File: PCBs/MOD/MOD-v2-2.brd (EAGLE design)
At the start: 138.8 x 49.3 mm, 32 parts, among them J1 SERVO1, J10 JOY1, J11 JOY2, J2 SERVO2, J4 ACTUATORS, J5 POWER-5V, J6 AN5, J7 AN6, J8 AN7, J9 AN8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

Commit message: added RPi power control circuitry
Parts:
- removed SW1: 500SSP1S2M2QEA, CMU-ArtFab:SWITCH_SPDT_500SSP1S2M2QEA
- added J12: RPi-Reset, SparkFun-Connectors:1X02_LOCK
- added J3: RPi, adafruit:DCJACK_2MM_PTH
- added R2: 2.2k, resistor:0204/7
- added R3: 3.3k, resistor:0204/7
- added RELAY1: RELAY-OMRON-G6DN, CMU-ArtFab:G6DN-1A
- added SW2: 500SSP1S2M2QEA, CMU-ArtFab:SWITCH_SPDT_500SSP1S2M2QEA
- added U1: ATTINY85SU, attiny85:ATTINY85
- J5: value POWER-5V -> Battery
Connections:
- removed net N$1: J5.PWR, SW1.2
- new net +5V-BATTERY: J5.PWR, RELAY1.5, SW2.1, U1.8
- new net +5V-PI: J3.PWR, RELAY1.8
- new net N$3: SW2.2, U1.5
- new net N$4: RELAY1.1, U1.7
- new net N$5: J12.1, R2.1, R3.2
- new net PI-REST: R2.2, U1.6
- net +5V: now also U1.3; no longer SW1.1
- net GND: now also J12.2, J3.GND, R3.1, RELAY1.2, SW2.3, U1.4
- net GNDBREAK: now also J3.GNDBREAK
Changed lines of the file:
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@@
 <?xml version="1.0" encoding="utf-8"?>
 <!DOCTYPE eagle SYSTEM "eagle.dtd">
-<eagle version="8.2.2">
+<eagle version="8.3.1">
 <drawing>
 <settings>
 <setting alwaysvectorfont="no"/>
+<setting keepoldvectorfont="yes"/>
 <setting verticaltext="up"/>
 </settings>
@@
 <attribute name="VALUE" x="139.381" y="30.868" size="1.016" layer="28" font="vector" ratio="20" rot="MR270"/>
 </element>
-<element name="J5" library="adafruit" package="DCJACK_2MM_PTH" value="POWER-5V" x="139.612" y="41.774" smashed="yes" rot="MR270">
+<element name="J5" library="adafruit" package="DCJACK_2MM_PTH" value="Battery" x="139.612" y="41.774" smashed="yes" rot="MR270">
 <attribute name="NAME" x="126.912" y="46.727" size="1.016" layer="26" font="vector" ratio="15" rot="MR0"/>
 <attribute name="VALUE" x="135.294" y="46.727" size="1.016" layer="28" font="vector" ratio="15" rot="MR0"/>
@@
 <attribute name="NAME" x="73.57799375" y="4.424896875" size="0.9906" layer="26" ratio="10" rot="MR270"/>
 <attribute name="VALUE" x="75.5356" y="7.102603125" size="0.9906" layer="28" ratio="10" rot="MR270"/>
-</element>
-<element name="SW1" library="CMU-ArtFab" package="SWITCH_SPDT_500SSP1S2M2QEA" value="500SSP1S2M2QEA" x="68.804" y="6.477" rot="R270">
-<attribute name="DIGIKEY" value="EG5137-ND" x="68.804" y="6.477" size="1.016" layer="27" font="vector" ratio="15" rot="R270" display="off"/>
 </element>
 <element name="TEENSY" library="CMU-ArtFab" package="TEENSY3-6_NO-USB-HOST" value="TEENSY3_6-ALI_NO-USB-HOST" x="99.904" y="18.34" rot="MR0"/>
@@
 <element name="S3" library="CMU-ArtFab" package="SWITCH_TR2-MOMENTARY-LED" value="SW-LEDPTH" x="108" y="4"/>
 <element name="S4" library="CMU-ArtFab" package="SWITCH_TR2-MOMENTARY-LED" value="SW-LEDPTH" x="128" y="4"/>
+<element name="U1" library="attiny85" package="ATTINY85" value="ATTINY85SU" x="-21" y="-4"/>
+<element name="RELAY1" library="CMU-ArtFab" package="G6DN-1A" value="RELAY-OMRON-G6DN" x="-21" y="-18"/>
+<element name="J3" library="adafruit" package="DCJACK_2MM_PTH" value="RPi" x="-50" y="-13"/>
+<element name="SW2" library="CMU-ArtFab" package="SWITCH_SPDT_500SSP1S2M2QEA" value="500SSP1S2M2QEA" x="-54" y="-38">
+<attribute name="DIGIKEY" value="EG5137-ND" x="-54" y="-38" size="1.778" layer="27" display="off"/>
+</element>
+<element name="R2" library="resistor" library_urn="urn:adsk.eagle:library:348" package="0204/7" value="2.2k" x="-60" y="-57"/>
+<element name="R3" library="resistor" library_urn="urn:adsk.eagle:library:348" package="0204/7" value="3.3k" x="-60" y="-71"/>
+<element name="J12" library="SparkFun-Connectors" library_urn="urn:adsk.eagle:library:513" package="1X02_LOCK" package3d_urn="urn:adsk.eagle:package:38045/1" value="RPi-Reset" x="-61" y="-88"/>
 </elements>
 <signals>
@@
 <contactref element="J2" pad="1"/>
 <contactref element="J4" pad="10"/>
-<contactref element="J5" pad="GND"/>
-<contactref element="LED1" pad="K"/>
 <contactref element="TEENSY" pad="G2"/>
 <contactref element="TEENSY" pad="G3"/>
@@
 <contactref element="S4" pad="C"/>
 <contactref element="S4" pad="1"/>
+<contactref element="U1" pad="4"/>
+<contactref element="RELAY1" pad="2"/>
+<contactref element="J5" pad="GND"/>
+<contactref element="SW2" pad="3"/>
+<contactref element="LED1" pad="K"/>
+<contactref element="J3" pad="GND"/>
+<contactref element="R3" pad="1"/>
+<contactref element="J12" pad="2"/>
+<wire x1="128.119" y1="32.99" x2="132.262" y2="41.774" width="0" layer="19" extent="1-1"/>
+<wire x1="125.539" y1="32.94" x2="128.119" y2="32.99" width="0" layer="19" extent="1-1"/>
+<wire x1="116.447" y1="32.377" x2="125.539" y2="32.94" width="0" layer="19" extent="1-1"/>
+<wire x1="118.65" y1="43.187" x2="116.447" y2="32.377" width="0" layer="19" extent="1-1"/>
+<wire x1="98.18" y1="43.187" x2="118.65" y2="43.187" width="0" layer="19" extent="1-1"/>
+<wire x1="77.69" y1="43.177" x2="98.18" y2="43.187" width="0" layer="19" extent="1-1"/>
+<wire x1="63.074" y1="34.85" x2="77.69" y2="43.177" width="0" layer="19" extent="1-1"/>
+<wire x1="57.22" y1="43.177" x2="63.074" y2="34.85" width="0" layer="19" extent="1-1"/>
+<wire x1="52.914" y1="27.23" x2="63.074" y2="34.85" width="0" layer="19" extent="1-1"/>
+<wire x1="40.214" y1="27.23" x2="52.914" y2="27.23" width="0" layer="19" extent="1-1"/>
+<wire x1="36.79" y1="43.157" x2="40.214" y2="27.23" width="0" layer="19" extent="1-1"/>
+<wire x1="83.394" y1="27.23" x2="77.69" y2="43.177" width="0" layer="19" extent="1-1"/>
+<wire x1="98.634" y1="19.61" x2="83.394" y2="27.23" width="0" layer="19" extent="1-1"/>
+<wire x1="89.8" y1="11.205" x2="98.634" y2="19.61" width="0" layer="19" extent="16-16"/>
+<wire x1="68.824" y1="16.619" x2="83.394" y2="27.23" width="0" layer="19" extent="1-1"/>
+<wire x1="108" y1="1.46" x2="98.634" y2="19.61" width="0" layer="19" extent="1-1"/>
+<wire x1="110.54" y1="1.46" x2="108" y2="1.46" width="0" layer="19" extent="1-1"/>
+<wire x1="128" y1="1.46" x2="110.54" y2="1.46" width="0" layer="19" extent="1-1"/>
+<wire x1="130.54" y1="1.46" x2="128" y2="1.46" width="0" layer="19" extent="1-1"/>
+<wire x1="16.36" y1="43.157" x2="36.79" y2="43.157" width="0" layer="19" extent="1-1"/>
+<wire x1="49.14" y1="2.255" x2="68.824" y2="16.619" width="0" layer="19" extent="16-16"/>
+<wire x1="32.54" y1="2.46" x2="49.14" y2="2.255" width="0" layer="19" extent="16-16"/>
+<wire x1="30" y1="2.46" x2="32.54" y2="2.46" width="0" layer="19" extent="1-1"/>
+<wire x1="12.54" y1="2.46" x2="30" y2="2.46" width="0" layer="19" extent="1-1"/>
+<wire x1="10" y1="2.46" x2="12.54" y2="2.46" width="0" layer="19" extent="1-1"/>
+<wire x1="-19.095" y1="-7.33" x2="10" y2="2.46" width="0" layer="19" extent="1-1"/>
+<wire x1="-18.46" y1="-18" x2="-19.095" y2="-7.33" width="0" layer="19" extent="1-1"/>
+<wire x1="-50" y1="-5.65" x2="-19.095" y2="-7.33" width="0" layer="19" extent="1-1"/>
+<wire x1="-49.3" y1="-38" x2="-50" y2="-5.65" width="0" layer="19" extent="1-1"/>
+<wire x1="-63.81" y1="-71" x2="-49.3" y2="-38" width="0" layer="19" extent="1-1"/>
+<wire x1="-58.2822" y1="-88" x2="-63.81" y2="-71" width="0" layer="19" extent="1-1"/>
 </signal>
 <signal name="B1">
@@
 <contactref element="J4" pad="7"/>
 <contactref element="J4" pad="8"/>
+<contactref element="U1" pad="3"/>
 <contactref element="R1" pad="2"/>
-<contactref element="SW1" pad="1"/>
+<wire x1="125.285" y1="30.4" x2="127.865" y2="30.45" width="0" layer="19" extent="1-1"/>
+<wire x1="113.907" y1="29.583" x2="125.285" y2="30.4" width="0" layer="19" extent="1-1"/>
+<wire x1="113.907" y1="32.377" x2="113.907" y2="29.583" width="0" layer="19" extent="1-1"/>
+<wire x1="75.053" y1="1.667" x2="113.907" y2="29.583" width="0" layer="19" extent="1-1"/>
+<wire x1="-20.365" y1="-7.33" x2="75.053" y2="1.667" width="0" layer="19" extent="1-1"/>
 </signal>
 <signal name="S1">
@@
 <signal name="GNDBREAK">
 <contactref element="J5" pad="GNDBREAK"/>
-</signal>
-<signal name="N$1">
-<contactref element="J5" pad="PWR"/>
-<contactref element="SW1" pad="2"/>
-<wire x1="68.804" y1="6.477" x2="126.012" y2="41.774" width="0" layer="19" extent="1-1"/>
+<contactref element="J3" pad="GNDBREAK"/>
+<wire x1="-45.2" y1="-2.25" x2="128.862" y2="36.974" width="0" layer="19" extent="1-1"/>
 </signal>
 <signal name="N$2">
@@
 <contactref element="U$1" pad="9"/>
 <contactref element="U$2" pad="9"/>
+<wire x1="58.74" y1="2.255" x2="80.2" y2="11.205" width="0" layer="19" extent="16-16"/>
 </signal>
 <signal name="N$11">
@@
 <contactref element="TEENSY" pad="46"/>
 <wire x1="42.754" y1="27.23" x2="108.827" y2="32.377" width="0" layer="19" extent="1-1"/>
+</signal>
+<signal name="N$3">
+<contactref element="U1" pad="5"/>
+<contactref element="SW2" pad="2"/>
+<wire x1="-19.095" y1="-0.67" x2="-54" y2="-38" width="0" layer="19" extent="1-1"/>
+</signal>
+<signal name="+5V-PI">
+<contactref element="RELAY1" pad="8"/>
+<contactref element="J3" pad="PWR"/>
+<wire x1="-3.22" y1="-18" x2="-50" y2="0.6" width="0" layer="19" extent="1-1"/>
+</signal>
+<signal name="PI-REST">
+<contactref element="U1" pad="6"/>
+<contactref element="R2" pad="2"/>
+<wire x1="-20.365" y1="-0.67" x2="-56.19" y2="-57" width="0" layer="19" extent="1-1"/>
+</signal>
+<signal name="+5V-BATTERY">
+<contactref element="U1" pad="8"/>
+<contactref element="J5" pad="PWR"/>
+<contactref element="SW2" pad="1"/>
+<contactref element="RELAY1" pad="5"/>
+<wire x1="-10.84" y1="-18" x2="126.012" y2="41.774" width="0" layer="19" extent="1-1"/>
+<wire x1="-22.905" y1="-0.67" x2="-10.84" y2="-18" width="0" layer="19" extent="1-1"/>
+<wire x1="-58.7" y1="-38" x2="-22.905" y2="-0.67" width="0" layer="19" extent="1-1"/>
+</signal>
+<signal name="N$4">
+<contactref element="U1" pad="7"/>
+<contactref element="RELAY1" pad="1"/>
+<wire x1="-21.635" y1="-0.67" x2="-21" y2="-18" width="0" layer="19" extent="1-1"/>
+</signal>
+<signal name="N$5">
+<contactref element="R2" pad="1"/>
+<contactref element="R3" pad="2"/>
+<contactref element="J12" pad="1"/>
+<wire x1="-56.19" y1="-71" x2="-61.1778" y2="-88" width="0" layer="19" extent="1-1"/>
+<wire x1="-63.81" y1="-57" x2="-56.19" y2="-71" width="0" layer="19" extent="1-1"/>
 </signal>
 </signals>
@@
 </note>
 <note version="8.2" severity="warning">
-Since Version 8.2, Eagle supports online libraries. The ids
+Since Version 8.2, EAGLE supports online libraries. The ids
 of those online libraries will not be understood (or retained)
 with this version.
 </note>
+<note version="8.3" severity="warning">
+Since Version 8.3, EAGLE supports URNs for individual library
+assets (packages, symbols, and devices). The URNs of those assets
+will not be understood (or retained) with this version.
+</note>
+<note version="8.3" severity="warning">
+Since Version 8.3, EAGLE supports the association of 3D packages
+with devices in libraries, schematics, and board files. Those 3D
+packages will not be understood (or retained) with this version.
+</note>
 </compatibility>

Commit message: added RPi power control circuitry
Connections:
- removed net +5V-PI: J3.PWR, RELAY1.8
- net +5V: now also J3.PWR, RELAY1.8
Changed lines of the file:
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@@
 <contactref element="U1" pad="3"/>
 <contactref element="R1" pad="2"/>
+<contactref element="RELAY1" pad="8"/>
+<contactref element="J3" pad="PWR"/>
 <wire x1="125.285" y1="30.4" x2="127.865" y2="30.45" width="0" layer="19" extent="1-1"/>
 <wire x1="113.907" y1="29.583" x2="125.285" y2="30.4" width="0" layer="19" extent="1-1"/>
 <wire x1="113.907" y1="32.377" x2="113.907" y2="29.583" width="0" layer="19" extent="1-1"/>
 <wire x1="75.053" y1="1.667" x2="113.907" y2="29.583" width="0" layer="19" extent="1-1"/>
-<wire x1="-20.365" y1="-7.33" x2="75.053" y2="1.667" width="0" layer="19" extent="1-1"/>
+<wire x1="-3.22" y1="-18" x2="75.053" y2="1.667" width="0" layer="19" extent="1-1"/>
+<wire x1="-20.365" y1="-7.33" x2="-3.22" y2="-18" width="0" layer="19" extent="1-1"/>
+<wire x1="-50" y1="0.6" x2="-20.365" y2="-7.33" width="0" layer="19" extent="1-1"/>
 </signal>
 <signal name="S1">
@@
 <wire x1="-19.095" y1="-0.67" x2="-54" y2="-38" width="0" layer="19" extent="1-1"/>
 </signal>
-<signal name="+5V-PI">
-<contactref element="RELAY1" pad="8"/>
-<contactref element="J3" pad="PWR"/>
-<wire x1="-3.22" y1="-18" x2="-50" y2="0.6" width="0" layer="19" extent="1-1"/>
-</signal>
 <signal name="PI-REST">

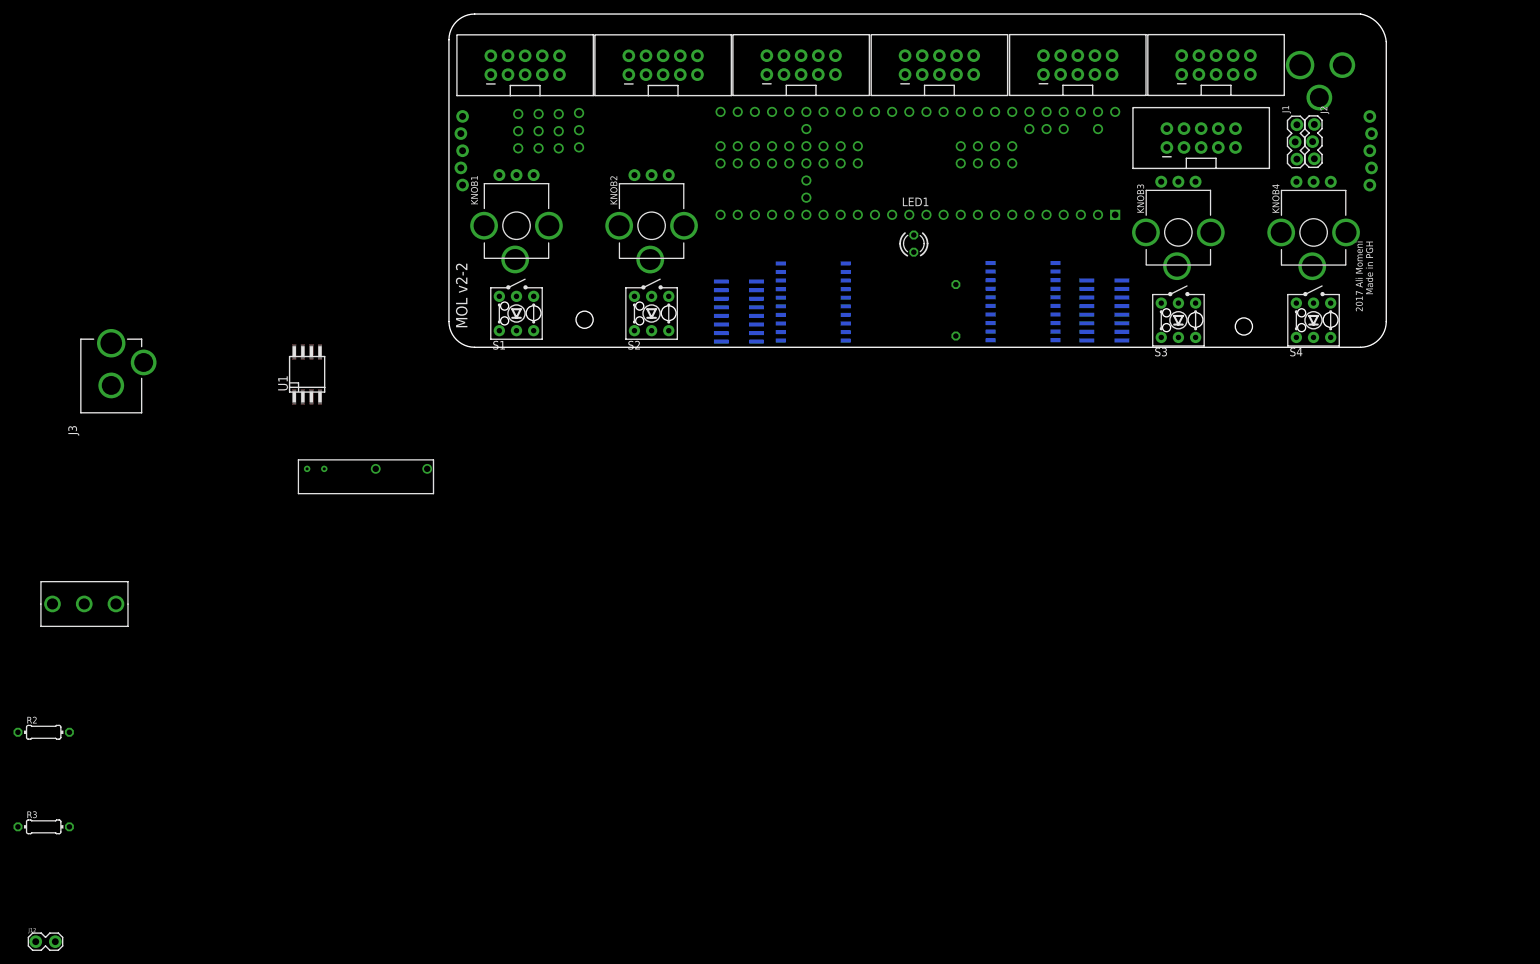
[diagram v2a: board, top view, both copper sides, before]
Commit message: attiny added to MOD pcb
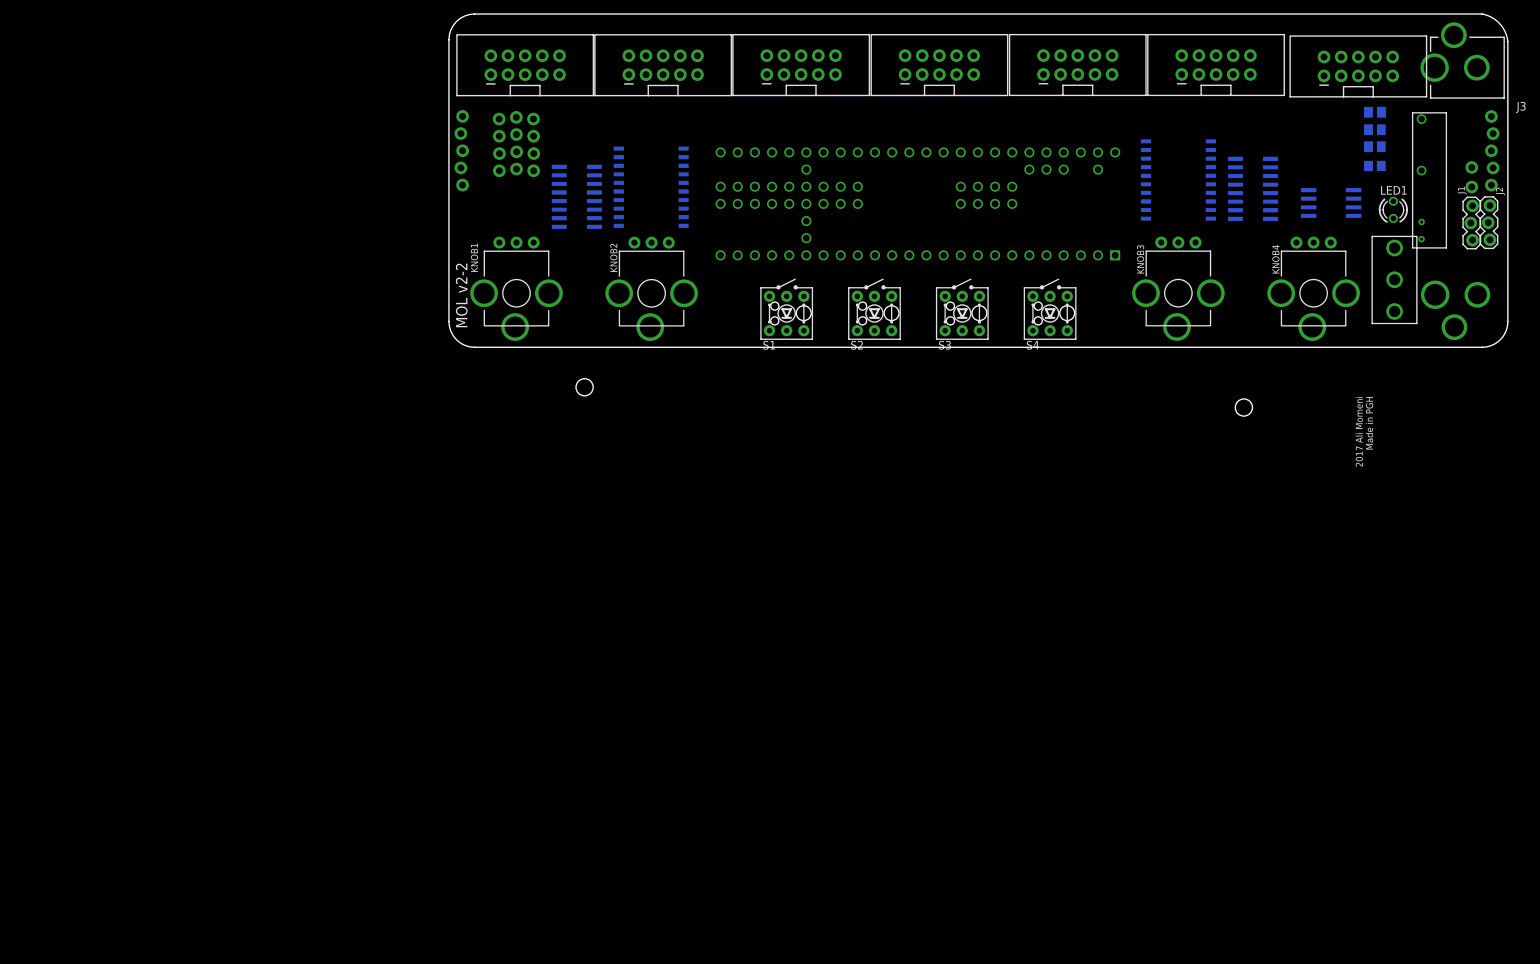
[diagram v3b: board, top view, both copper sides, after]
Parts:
- added C1: 10uF, resistor:C0805
- J12: value RPi-Reset -> RPi-Shutdown
- J6, J7, J8, J9: device SparkFun-Connectors:1X03_NO_SILK -> SparkFun-Connectors:1X03_LOCK
- R1: device resistor:0204/7 -> rcl:M0805
- R2: value 2.2k -> 2.2K; device resistor:0204/7 -> rcl:M0805
- R3: value 3.3k -> 3.3K; device resistor:0204/7 -> rcl:M0805
- U1: value ATTINY85SU -> ATTINY85
- moved J12 241.3 mm to (151.4, 26.4), flipped to the bottom, turned to 270 degrees
- moved R3 223.7 mm to (137.1, 34.8), flipped to the bottom
- moved J3 216.5 mm to (159.5, 41.4), turned to 90 degrees
- moved R2 216.3 mm to (137.1, 32.2), flipped to the bottom, turned to 180 degrees
- moved SW2 199.8 mm to (140.0, 10.0), turned to 270 degrees
- moved RELAY1 168.5 mm to (144.0, 16.0), turned to 90 degrees
- moved U1 153.7 mm to (130.6, 21.4), flipped to the bottom, turned to 270 degrees
- moved LED1 71.2 mm to (139.8, 20.3)
- moved R1 66.6 mm to (137.1, 29.7), turned to 0 degrees
- moved S1 40.0 mm to (50.0, 5.00)
- moved J5 39.4 mm to (159.6, 7.77)
- moved S4 39.0 mm to (89.0, 5.00)
- moved S2 33.0 mm to (63.0, 5.00)
- moved S3 32.0 mm to (76.0, 5.00)
- moved RN2 29.4 mm to (18.9, 22.3)
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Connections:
- net +5V: now also R1.1; no longer R1.2
- net +5V-BATTERY: now also C1.1
- net GND: now also C1.2, R3.2; no longer R3.1
- net N$2: now also R1.2; no longer R1.1
- net N$5: now also R2.2, R3.1; no longer R2.1, R3.2
- net PI-REST: now also R2.1; no longer R2.2
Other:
- board size 138.8 x 49.3 mm -> 156.8 x 49.3 mm
